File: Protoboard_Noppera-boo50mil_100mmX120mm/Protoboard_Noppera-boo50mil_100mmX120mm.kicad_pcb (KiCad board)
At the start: 2 copper layers, 99.6 x 119.6 mm, 0 parts

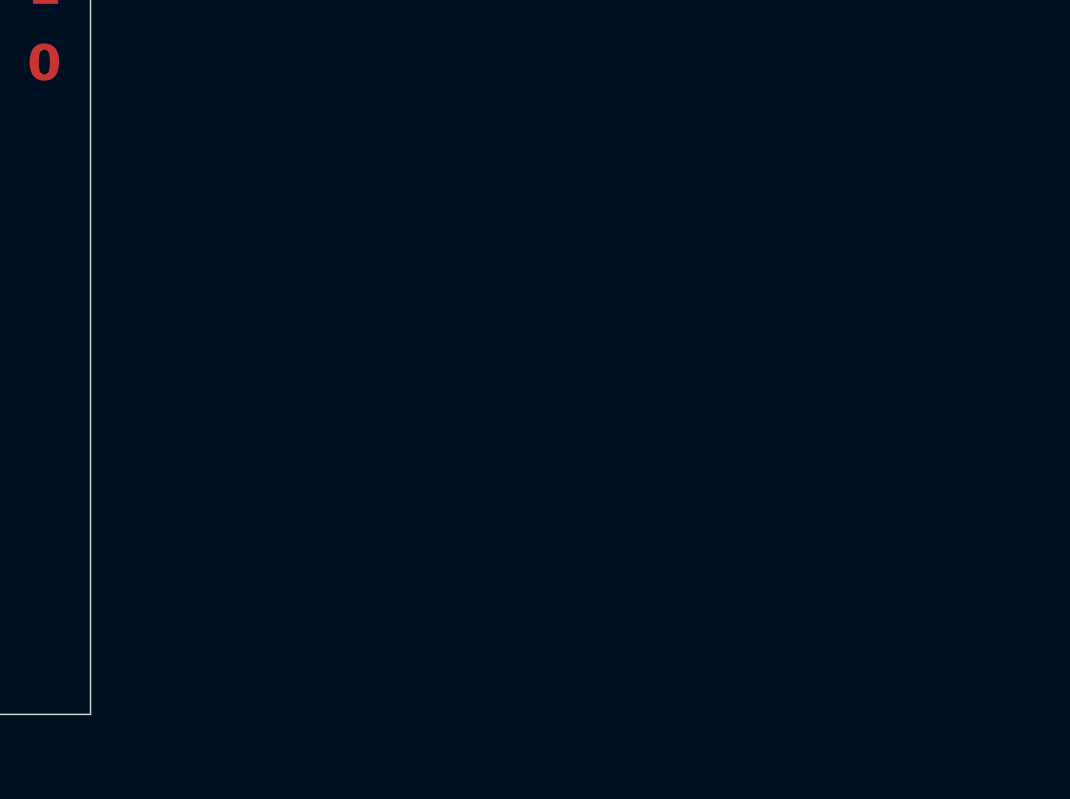
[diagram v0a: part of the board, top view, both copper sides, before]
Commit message: added dummy footprints for the tactile switch breakout and the 4mm banana jack breakout
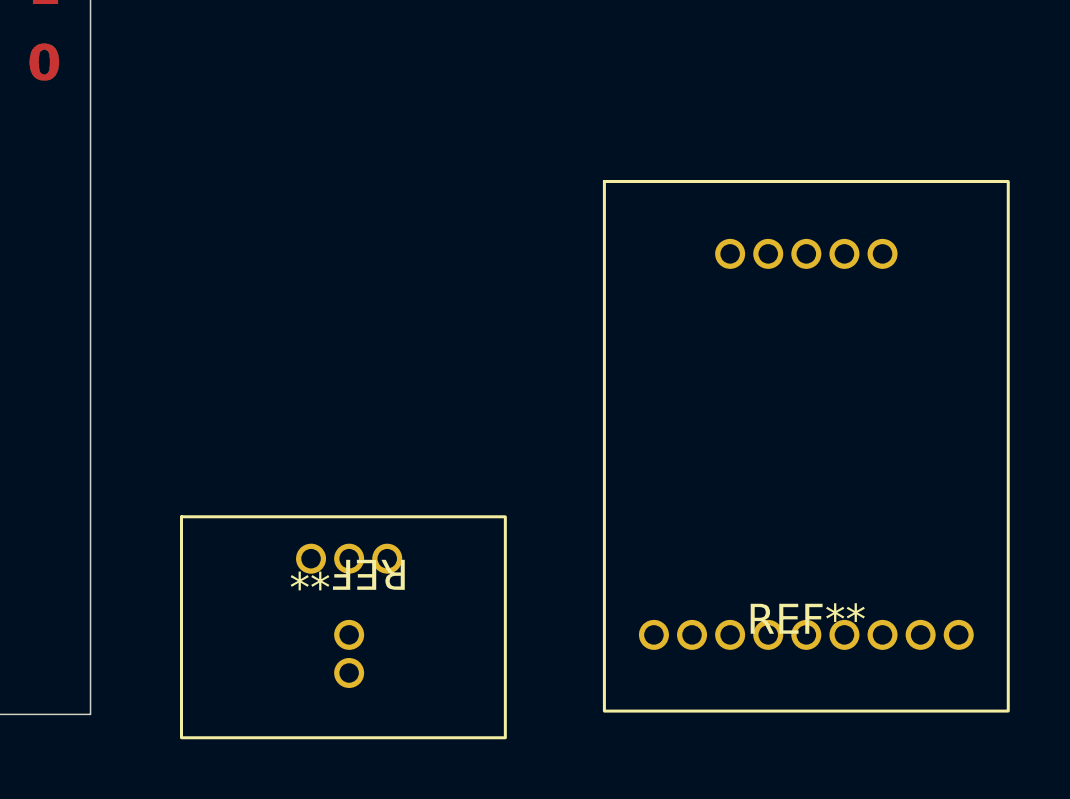
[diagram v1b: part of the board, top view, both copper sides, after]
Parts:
- added REF**: 4mm_banana_breakout, 4mm_banana_breakout:4mm_banana_breakout, F.Cu at (170.2, 156.2)
- added REF**: PTS645_breakout, PTS645_breakout:PTS645_breakout, F.Cu at (154.9, 157.5)

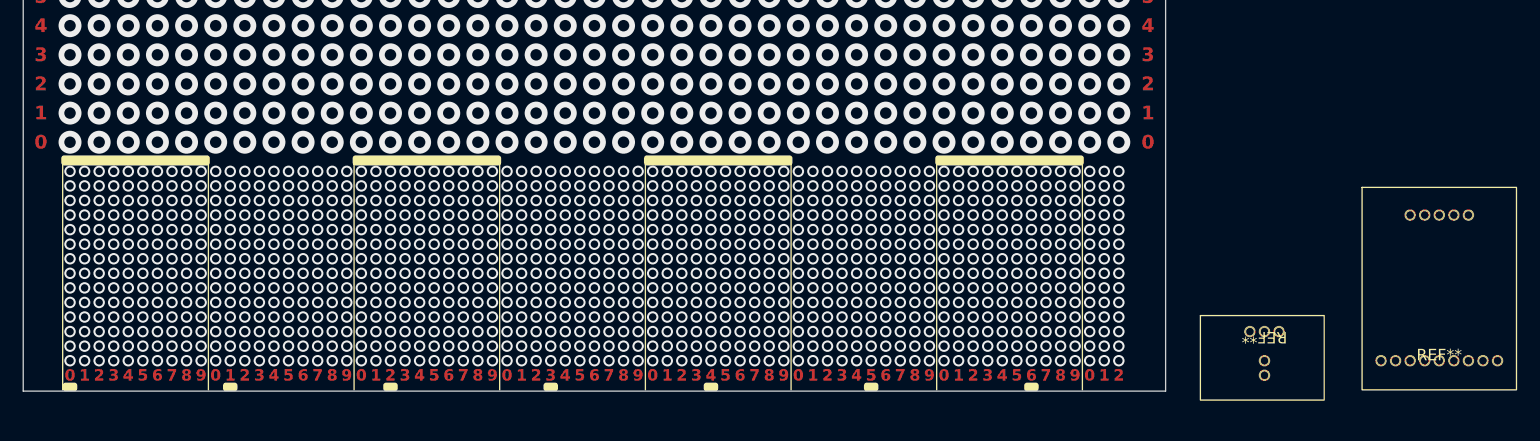
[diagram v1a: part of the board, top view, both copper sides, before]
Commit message: added missing dummy footprints, added examples to the protoboard
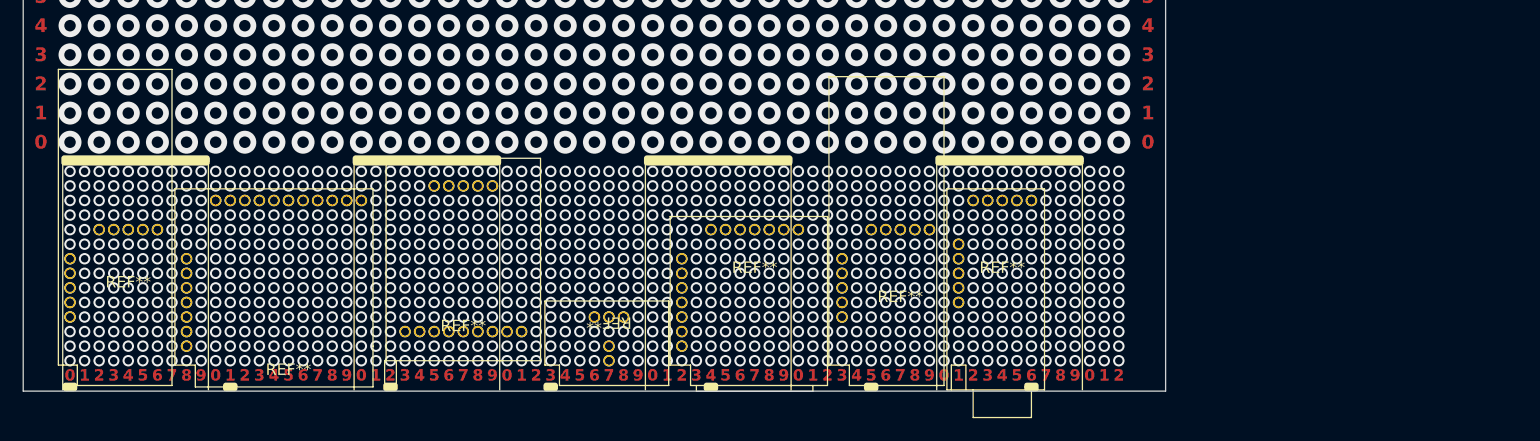
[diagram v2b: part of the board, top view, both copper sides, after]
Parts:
- added REF**: BNC_breakout, BNC_breakout:BNC_breakout, F.Cu at (69.8, 157.5)
- added REF**: IF-D91B_breakout, IF-D91B_breakout:IF-D91B_breakout, F.Cu at (55.9, 149.9)
- added REF**: SJ3-35083D-TR, SJ3-35083D-TR:SJ3-35083D-TR, F.Cu at (132.1, 148.6)
- added REF**: PJ-063AH_breakout, PJ-063AH_breakoutl:PJ-063AH_breakout, F.Cu at (110.5, 148.6)
- added REF**: IF-E96E_breakout, IF-E96E_breakout:IF-E96E_breakout, F.Cu at (123.2, 151.1)
- moved REF** 85.1 mm to (85.1, 153.7)
- moved REF** 57.2 mm to (97.8, 156.2)
